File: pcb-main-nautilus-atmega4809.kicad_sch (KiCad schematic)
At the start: 0 parts

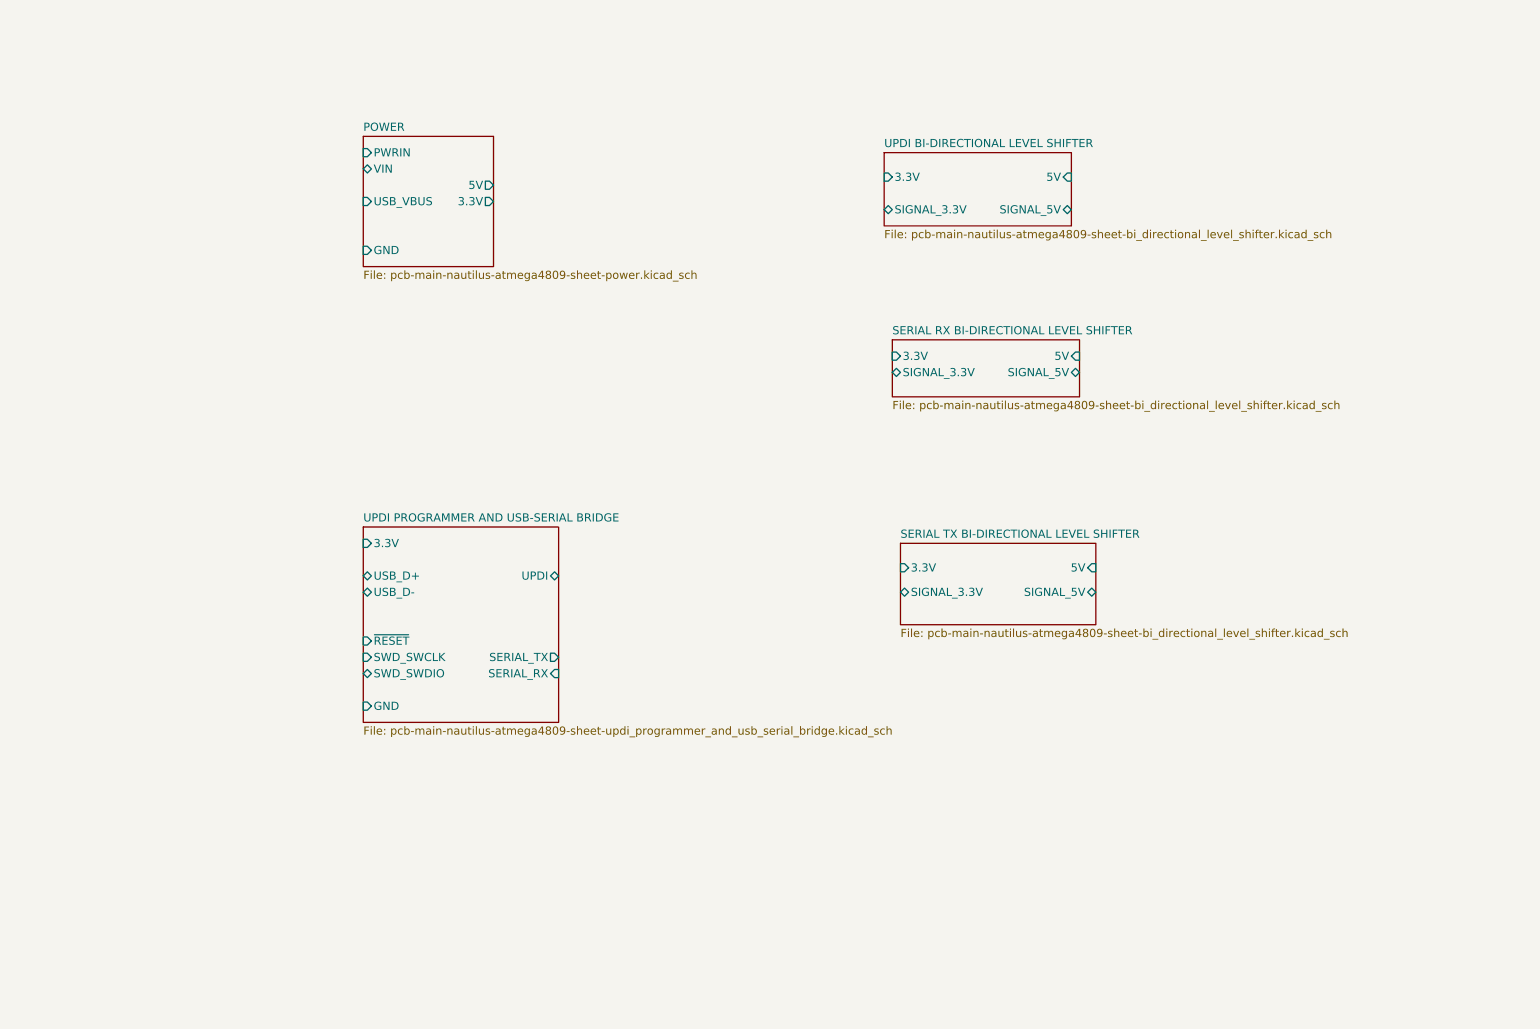
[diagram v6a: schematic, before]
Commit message: Add MCU sheet
Supports #2.
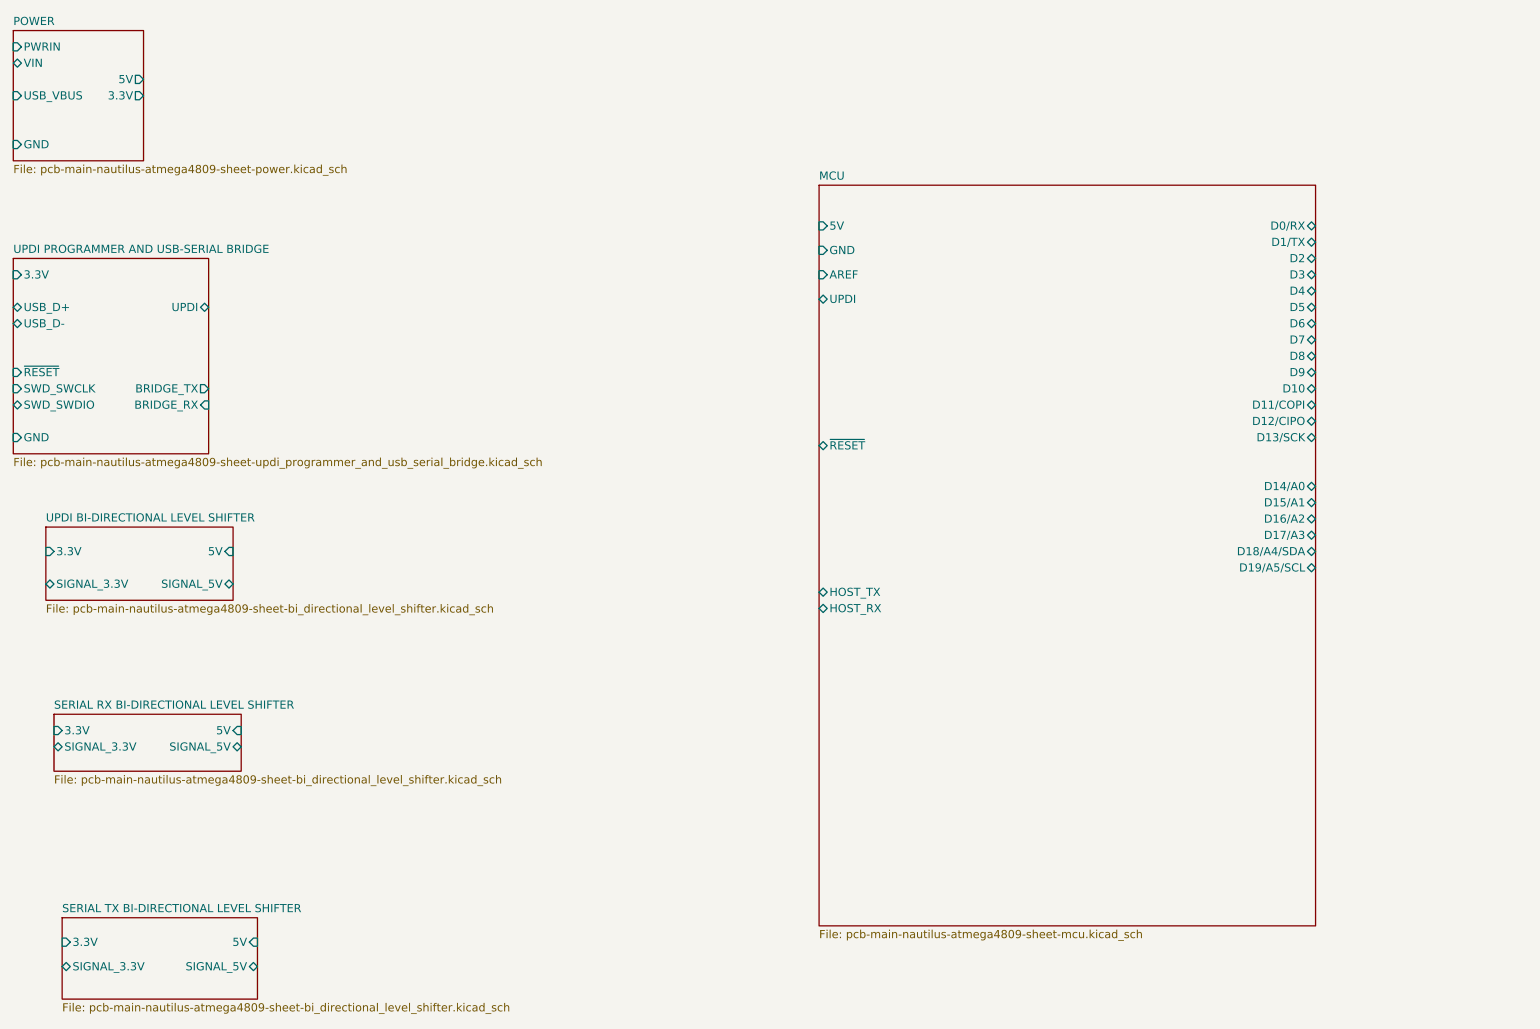
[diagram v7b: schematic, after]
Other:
- added sheet MCU (pcb-main-nautilus-atmega4809-sheet-mcu.kicad_sch)
- sheet UPDI PROGRAMMER AND USB-SERIAL BRIDGE ports: added BRIDGE_RX, BRIDGE_TX; removed SERIAL_RX, SERIAL_TX
